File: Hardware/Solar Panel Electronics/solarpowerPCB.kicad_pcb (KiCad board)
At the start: 4 copper layers, 46.2 x 77 mm, 145 parts, among them J1 Screw_Terminal_SolarPanel_Inp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, J10 Screw_Terminal_SolarPanel_Inp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, J11 Screw_Terminal_SolarPanel_Inp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, J12 NTC Connector, J13 Battery Connector, J14 Screw_Terminal_5VRail, J2 Screw_Terminal_SolarPanel_Inp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, J3 Conn_01x02_Male, J4 Conn_01x06_Male, J5 Conn_01x02_Male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

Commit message: Layed out parts a bit more
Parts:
- removed REF** (x4): MountingHole_2.2mm_M2, MountingHole:MountingHole_2.2mm_M2
- moved C9 129.8 mm to (153.8, 177.5)
- moved R19 128.0 mm to (169.3, 177.5)
- moved J3 128.0 mm to (156.4, 174.7)
- moved R6 125.1 mm to (153.8, 160.2), turned to -90 degrees
- moved D4 125.1 mm to (153.8, 163.2)
- moved C7 123.9 mm to (161.0, 166.5), turned to 90 degrees
- moved R17 123.9 mm to (162.5, 166.5), turned to -90 degrees
- moved Q1 123.6 mm to (164.2, 161.5), turned to 45 degrees
- moved R18 123.5 mm to (153.8, 174.5), turned to -90 degrees
- moved R4 123.5 mm to (165.8, 163.0), turned to 45 degrees
- moved R16 122.7 mm to (162.8, 160.0), turned to -135 degrees
- moved R7 120.6 mm to (152.2, 160.2)
- moved TP1 119.7 mm to (163.0, 155.2), turned to 90 degrees
- moved D5 119.5 mm to (152.2, 163.2), turned to 90 degrees
- moved U2 119.2 mm to (157.0, 153.9), turned to 135 degrees
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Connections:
- D8 pad 1: unconnected-(D8-Pad1) -> Net-(D8-Pad1)
- R11 pad 1: unconnected-(R11-Pad1) -> Net-(D8-Pad1)

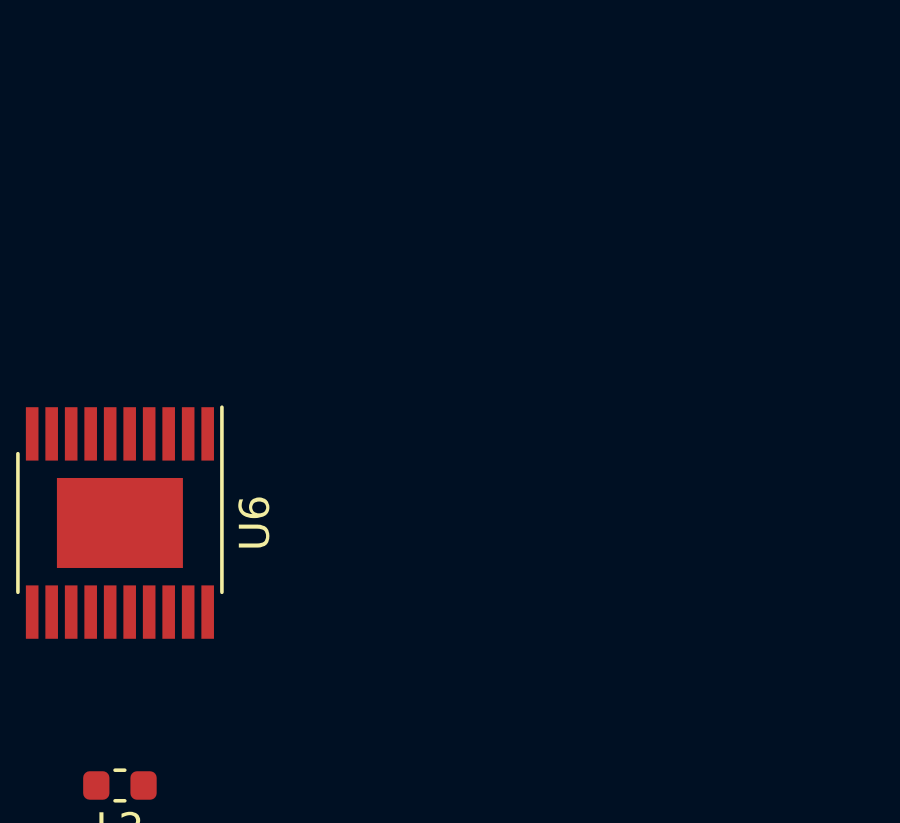
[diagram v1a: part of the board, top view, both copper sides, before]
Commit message: Sized the buck-boost converter components. Need to complete pcb layout.
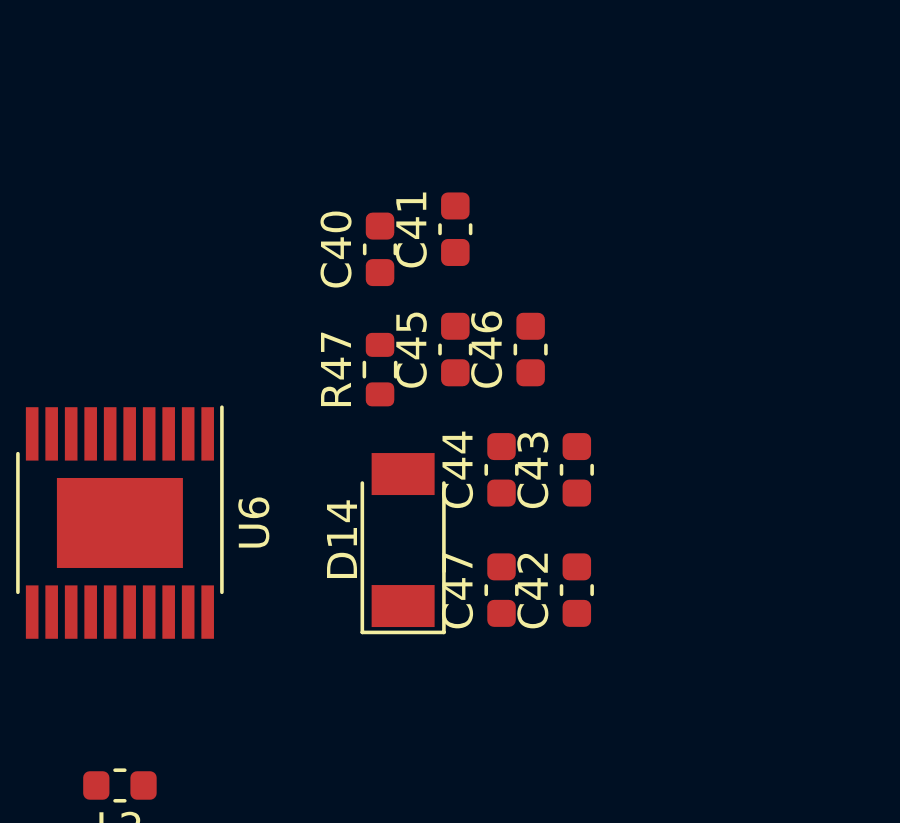
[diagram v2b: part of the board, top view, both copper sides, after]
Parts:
- added C40: 2.2u, Capacitor_SMD:C_0603_1608Metric, F.Cu at (153.7, 71.6)
- added C41: 2.2u, Capacitor_SMD:C_0603_1608Metric, F.Cu at (156.2, 71.0)
- added C42: 2.2u, Capacitor_SMD:C_0603_1608Metric, F.Cu at (160.2, 83.0)
- added C43: 2.2u, Capacitor_SMD:C_0603_1608Metric, F.Cu at (160.2, 79.0)
- added C44: 47u, Capacitor_SMD:C_0603_1608Metric, F.Cu at (157.7, 79.0)
- added C45: 47u, Capacitor_SMD:C_0603_1608Metric, F.Cu at (156.2, 75.0)
- added C46: 0.47u, Capacitor_SMD:C_0603_1608Metric, F.Cu at (158.7, 75.0)
- added C47: 0.47u, Capacitor_SMD:C_0603_1608Metric, F.Cu at (157.7, 83.0)
- added D14: D_Schottky_6V, Diode_SMD:D_SOD-128, F.Cu at (154.4, 81.3)
- added R47: 1M, Resistor_SMD:R_0603_1608Metric, F.Cu at (153.7, 75.6)
- C21: value C_Small -> 2.2u
- C22: value C_Small -> 1u
- C23, C25: value C_Small -> 0.1u
- C24: value C_Small -> 1.6n
- C26: value C -> 100nF
- C27: value C -> 2.2nF
- D13: value D_Schottky -> D_Schottky_10V_1.5A
- L2: value L -> 17uH
- R35: value R_Small -> 18.3k
- R36: value R_Small -> 15m
- R37: value R_Small -> 10k
- R38: value R_Small -> 900
- R39: value R_Small -> 300
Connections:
- L2 pad 2: /VoltageReg/V_reg -> Net-(L2-Pad2)
- Q2 pad 1: unconnected-(Q2-Pad1) -> /VSolCharger
- Q3 pad 1: /VoltageReg/V_reg -> Net-(L2-Pad2)
- U6 pad 4: /VSolCharger -> Net-(U6-Pad4)

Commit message: Need to do routing.
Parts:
- removed ANT1: AMCA31-2R450G-S1F-T3, iclr:ANT_AMCA31-2R450G-S1F-T3
- removed C38: 33pF, Capacitor_SMD:C_0603_1608Metric
- removed C39: 100pF, Capacitor_SMD:C_0603_1608Metric
- removed L3: LQG15WZ1N8B02D, Inductor_SMD:L_0603_1608Metric_Pad1.05x0.95mm_HandSolder
- added REF**: MountingHole_2.2mm_M2, MountingHole:MountingHole_2.2mm_M2, F.Cu at (80.0, 140.0)
- added REF**: MountingHole_2.2mm_M2, MountingHole:MountingHole_2.2mm_M2, F.Cu at (40.0, 141.0)
- added REF**: MountingHole_2.2mm_M2, MountingHole:MountingHole_2.2mm_M2, F.Cu at (40.0, 72.0)
- added REF**: MountingHole_2.2mm_M2, MountingHole:MountingHole_2.2mm_M2, F.Cu at (80.0, 72.0)
- C26: value 100nF -> 55nF
- C27: value 2.2nF -> 0.01nF
- R37: value 10k -> 17k
- U2: value ESP32-PICO-D4 -> ESP32-WROOM-32D; footprint Package_DFN_QFN:QFN-48-1EP_7x7mm_P0.5mm_EP5.3x5.3mm -> RF_Module:ESP32-WROOM-32
- moved R19 139.4 mm to (63.3, 87.0), turned to 0 degrees
- moved R17 126.5 mm to (62.3, 89.3), turned to 90 degrees
- moved R7 125.0 mm to (49.8, 88.6), turned to 0 degrees
- moved C1 124.7 mm to (52.5, 90.2), turned to 180 degrees
- moved C7 123.9 mm to (64.1, 89.3), turned to -90 degrees
- moved C2 123.6 mm to (53.0, 88.6), turned to 0 degrees
- moved TP1 123.5 mm to (58.1, 90.0)
- moved D3 123.0 mm to (49.4, 90.2), turned to 180 degrees
- moved D5 121.8 mm to (57.0, 87.4)
- moved D4 121.6 mm to (58.7, 87.4)
- moved R6 120.7 mm to (55.5, 90.2), turned to 0 degrees
- moved TP2 120.4 mm to (60.2, 90.0)
- moved R5 115.0 mm to (60.4, 87.4), turned to 90 degrees
- moved J3 112.7 mm to (70.4, 101.9), turned to 90 degrees
- moved U2 112.7 mm to (57.6, 101.0), turned to 90 degrees
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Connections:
- U2 pad 1: +3V3 -> GND
- U2 pad 11: unconnected-(U2-Pad11) -> /CAN_TX
- U2 pad 12: /CAN_TX -> /CAN_RX
- U2 pad 13: /CAN_RX -> /HSPI_SCLK
- U2 pad 14: /~{SD_CS} -> /HSPI_MISO
- U2 pad 15: /~{ADC_CS} -> GND
- U2 pad 16: unconnected-(U2-Pad16) -> /HSPI_MOSI
- U2 pad 17: /HSPI_SCLK -> unconnected-(U2-Pad17)
- U2 pad 18: /HSPI_MISO -> unconnected-(U2-Pad18)
- U2 pad 19: +3V3 -> unconnected-(U2-Pad19)
- U2 pad 2: /LNA -> +3V3
- U2 pad 20: /HSPI_MOSI -> unconnected-(U2-Pad20)
- U2 pad 21: /CLKOUT -> unconnected-(U2-Pad21)
- U2 pad 23: /BOOT -> /CLKOUT
- U2 pad 25: unconnected-(U2-Pad25) -> /BOOT
- U2 pad 27: unconnected-(U2-Pad27) -> /VSPI_SCLK
- U2 pad 28: unconnected-(U2-Pad28) -> /VSPI_MISO
- U2 pad 3: +3V3 -> /EN
- U2 pad 30: unconnected-(U2-Pad30) -> /SDA
- U2 pad 31: unconnected-(U2-Pad31) -> /SCL
- U2 pad 33: unconnected-(U2-Pad33) -> /VSPI_MOSI
- U2 pad 34: unconnected-(U2-Pad34) -> Net-(R7-Pad1)
- U2 pad 35: /VSPI_SCLK -> Net-(R6-Pad1)
- U2 pad 36: /VSPI_MOSI -> /~{SD_CS}
- U2 pad 37: +3V3 -> /~{ADC_CS}
- U2 pad 38: /VSPI_MISO -> GND
- U2 pad 39: /SCL -> GND
- U2 pad 4: +3V3 -> unconnected-(U2-Pad4)
- U2 pad 9: /EN -> unconnected-(U2-Pad9)
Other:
- board size 46.2 x 77 mm -> 49.7 x 77 mm

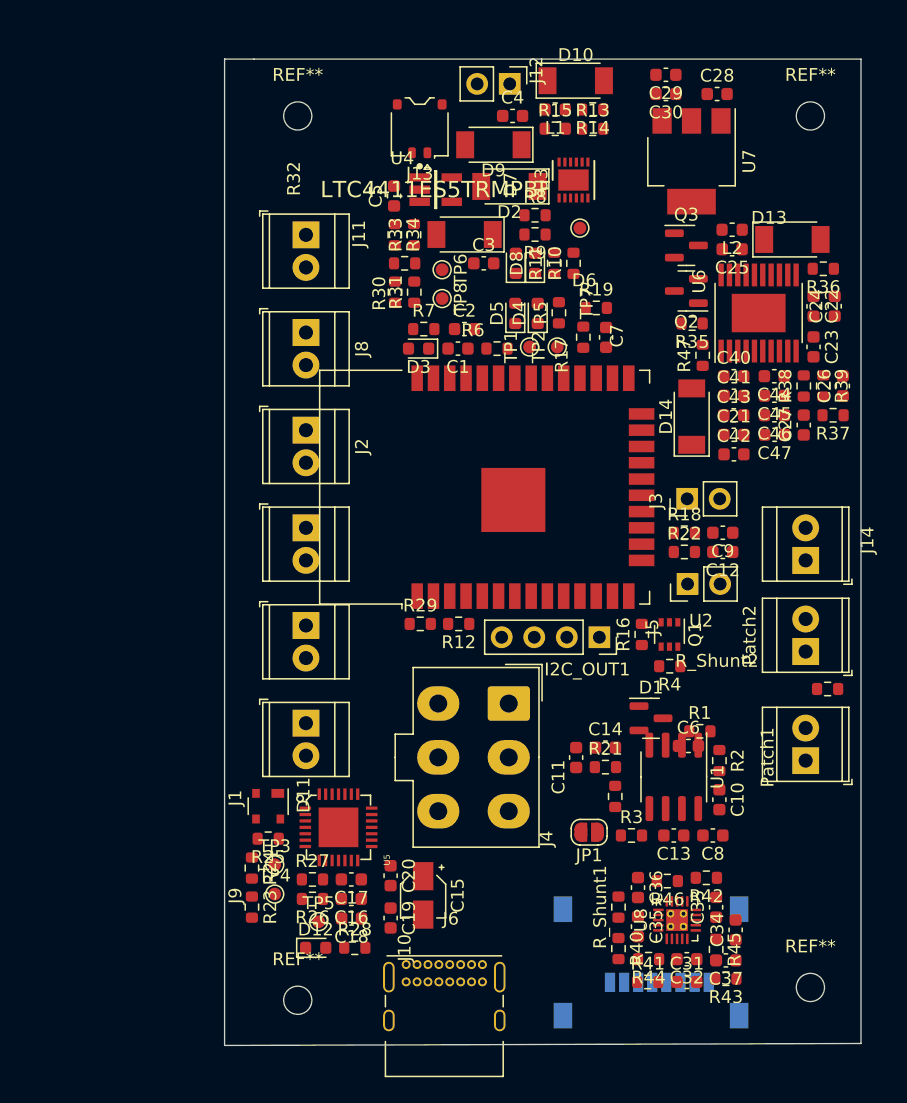
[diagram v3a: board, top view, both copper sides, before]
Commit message: New Layout (did not change subsystem layout)
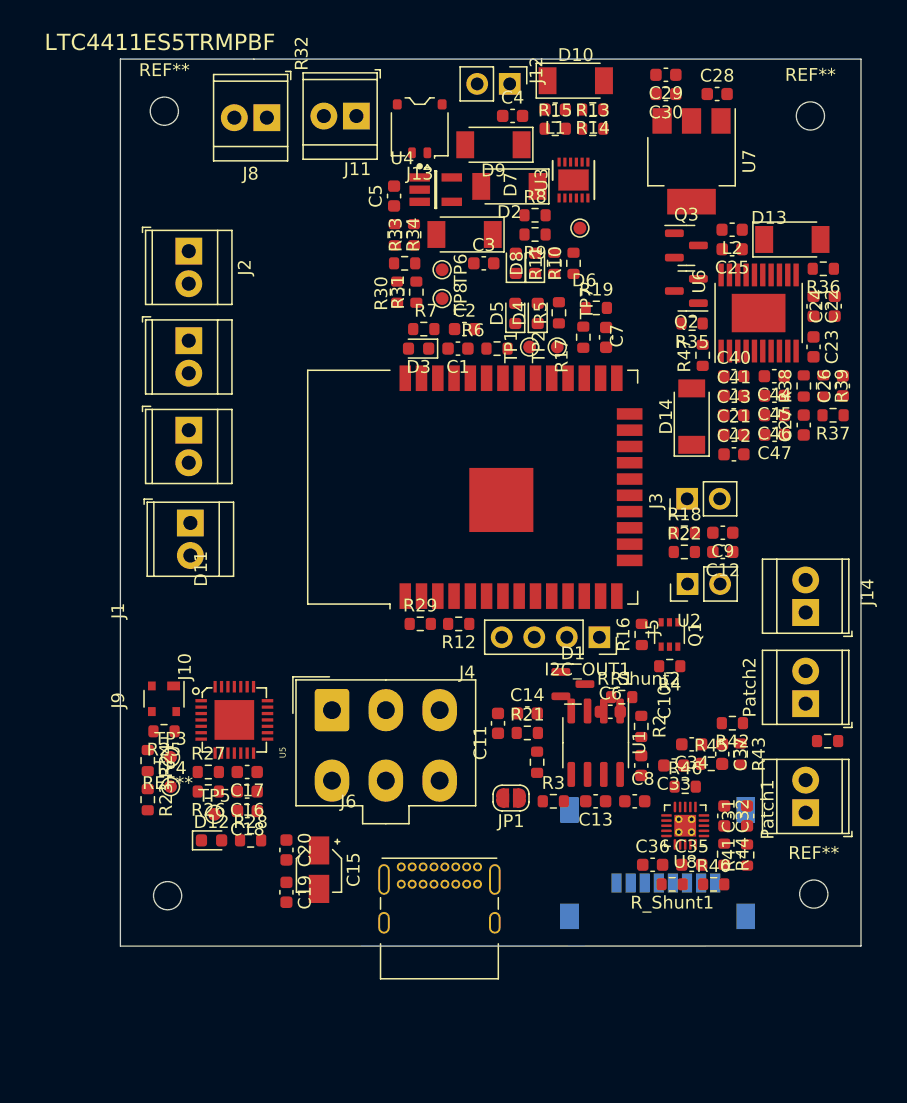
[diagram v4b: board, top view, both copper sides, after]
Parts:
- moved J10 18.0 mm to (31.6, 103.8)
- moved J9 17.8 mm to (31.5, 96.5)
- moved R43 17.6 mm to (74.5, 121.8), turned to -90 degrees
- moved J1 17.2 mm to (31.5, 89.5)
- moved J8 17.0 mm to (37.6, 72.1), turned to 180 degrees
- moved J2 16.7 mm to (31.5, 82.5)
- moved C37 16.1 mm to (73.1, 121.8), turned to -90 degrees
- moved C34 14.9 mm to (70.7, 121.0), turned to 180 degrees
- moved R45 14.5 mm to (72.3, 122.6), turned to 0 degrees
- moved J4 13.8 mm to (42.7, 118.4), turned to 0 degrees
- moved C31 13.8 mm to (75.1, 126.6), turned to 90 degrees
- moved REF** 13.0 mm to (29.8, 132.8)
- moved R41 12.6 mm to (75.1, 129.7), turned to 90 degrees
- moved R42 12.2 mm to (73.9, 119.4)
- moved C16 11.7 mm to (36.1, 124.7)
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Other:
- board size 49.7 x 77 mm -> 57.8 x 69.2 mm

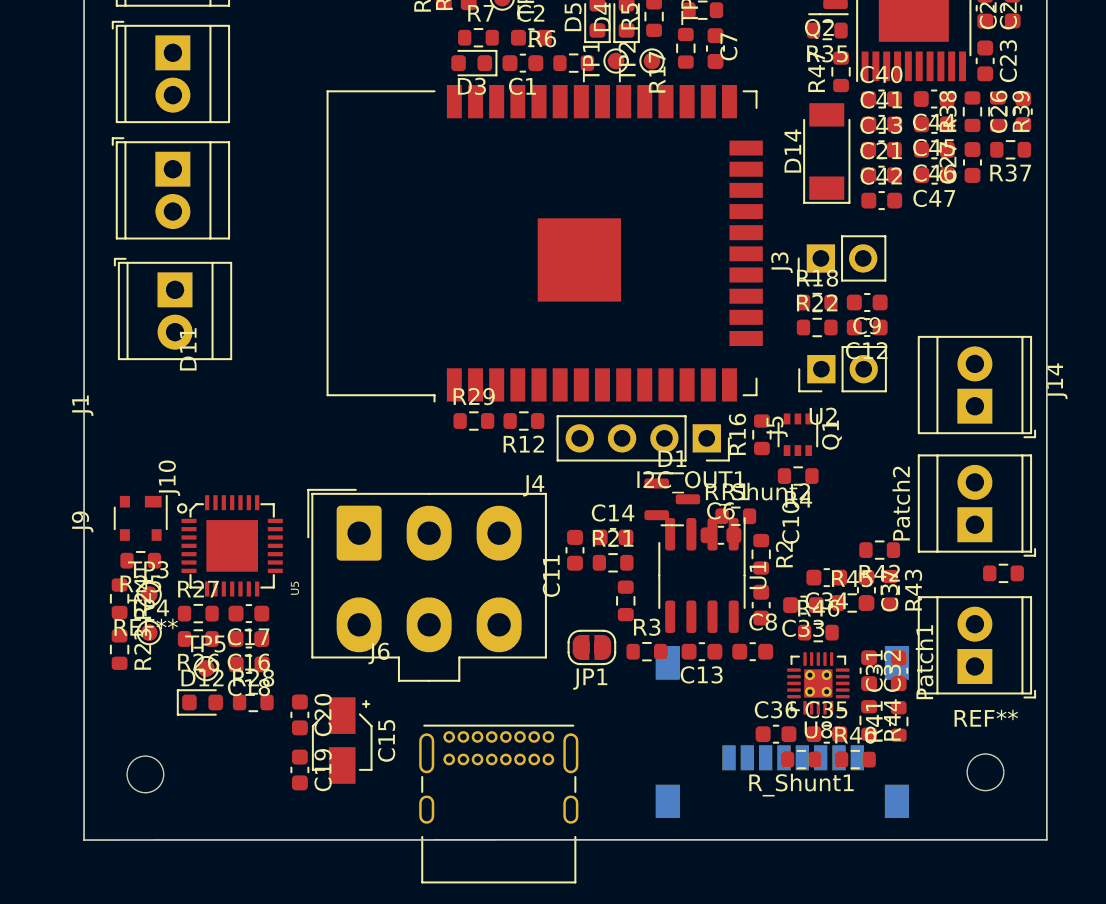
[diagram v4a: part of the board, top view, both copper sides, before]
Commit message: Partly done routing. Need to replace solar charging circuit
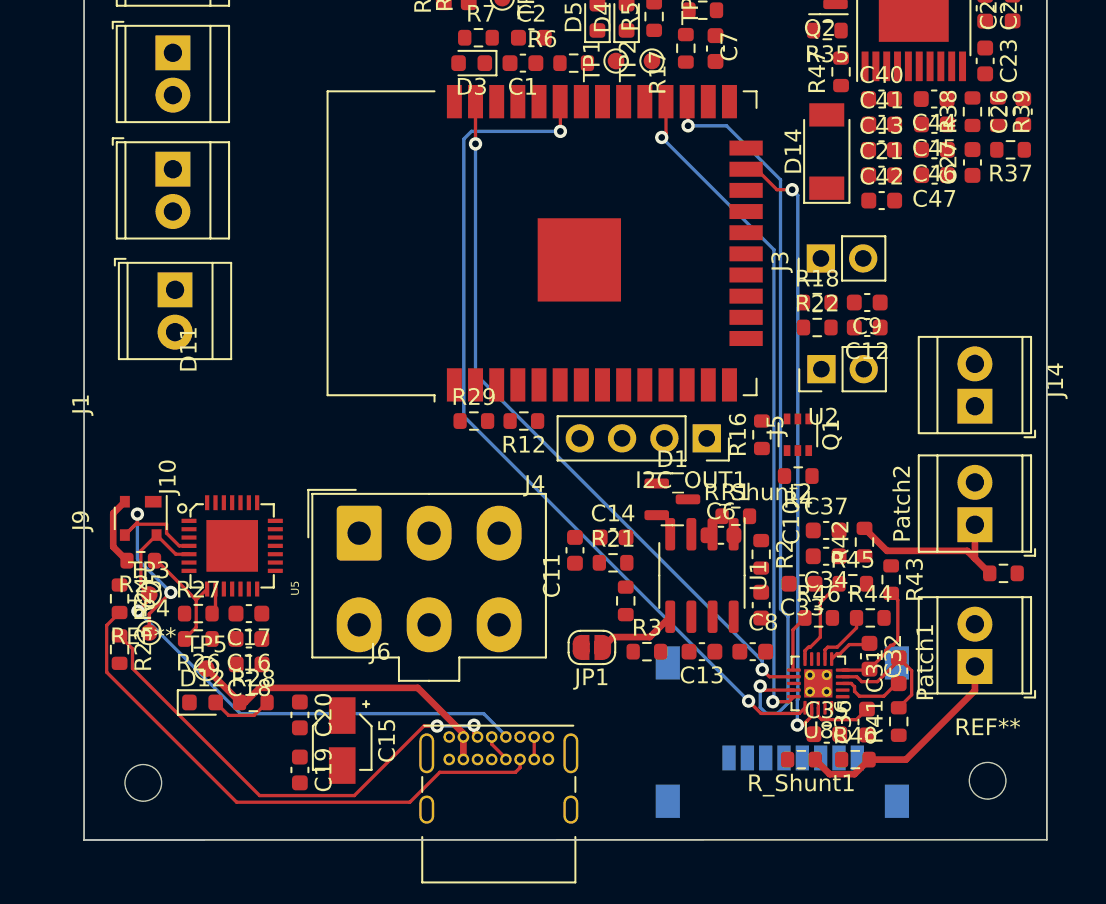
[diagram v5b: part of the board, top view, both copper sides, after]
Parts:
- moved R44 6.15 mm to (73.3, 123.5), turned to 0 degrees
- moved C36 5.51 mm to (73.2, 129.7), turned to 90 degrees
- moved C37 4.33 mm to (70.7, 118.2), turned to 0 degrees
- moved C33 1.29 mm to (69.2, 121.4)
- moved C34 1.28 mm to (70.7, 119.8)
- moved R45 1.16 mm to (72.3, 121.4)
- moved R42 1.03 mm to (73.0, 118.9), turned to 90 degrees
- moved R46 0.88 mm to (70.2, 123.5)
- moved C32 0.87 mm to (73.3, 125.8)
- moved R43 0.65 mm to (74.6, 121.2)
- moved REF** 0.52 mm to (80.4, 133.2)
- moved REF** 0.52 mm to (29.7, 133.3)
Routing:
- net /VSPI_MOSI: track 0.00 -> 52.4 mm, vias 0 -> 2
- net /VSPI_SCLK: track 0.00 -> 45.4 mm, vias 0 -> 2
- net /~{ADC_CS}: track 0.00 -> 43.3 mm, vias 0 -> 2
- net /VSPI_MISO: track 0.00 -> 40.3 mm, vias 0 -> 2
- net /CLKOUT: track 0.00 -> 37.1 mm, vias 0 -> 2
- net /usb_to_uart/Data-: track 0.00 -> 34.8 mm, vias 0 -> 1
- net Net-(J6-PadB5): track 0.00 -> 33.3 mm
- net Net-(J6-PadA5): track 0.00 -> 28.5 mm, vias 0 -> 2
- net VBUS: track 0.00 -> 24.9 mm
- net /usb_to_uart/Data+: track 0.00 -> 16.7 mm, vias 0 -> 2
- net Net-(Patch1-Pad1): track 0.00 -> 13.5 mm
- net Net-(Patch2-Pad1): track 0.00 -> 10.7 mm
- net /ADC/AIN0N: track 0.00 -> 7.80 mm
- net /ADC/AIN1N: track 0.00 -> 7.12 mm
- net Net-(R25-Pad1): track 0.00 -> 7.04 mm
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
